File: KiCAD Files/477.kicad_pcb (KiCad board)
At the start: 2 copper layers, 96 x 57.4 mm, 75 parts, among them IC1 W25N01GVSFIG, IC2 W25N01GVSFIG, IC3 W25N01GVSFIG, IC4 W25N01GVSFIG, IC5 AZ1117IH-3.3TRG1, IC6 USBLC6-2SC6, J1 BM06B-SRSS-TBT_LF__SN_, J2 6364372-2, J3 TSW-103-14-S-D, J4 TSW-103-14-S-D, J5 BM07B-SRSS-TB_LF__SN_, J6 BM09B-SRSS-TB_LF__SN_, J7 TSW-105-05-F-S, U1 STM32H7A3RGTx, Y1 ABM8G-48.000MHZ-18-D2Y-T

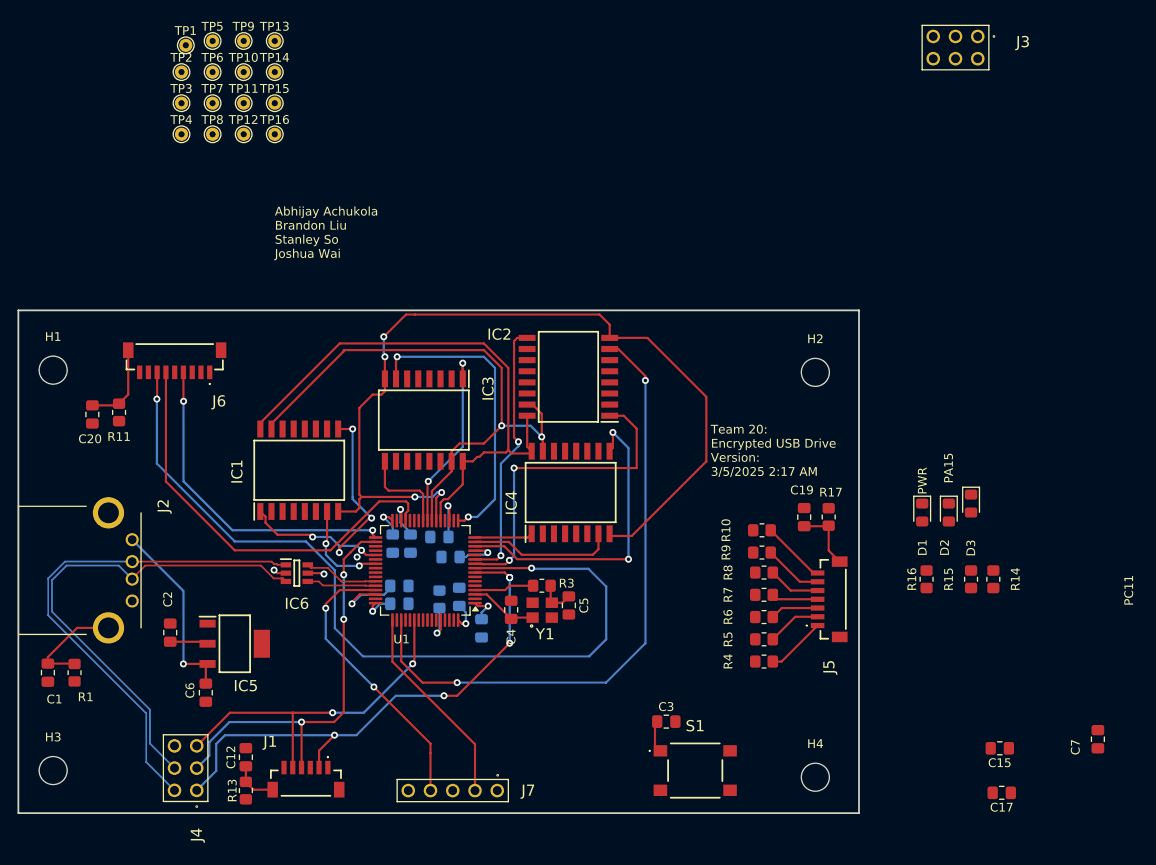
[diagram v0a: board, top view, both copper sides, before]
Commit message: added pcb routing for debug pins
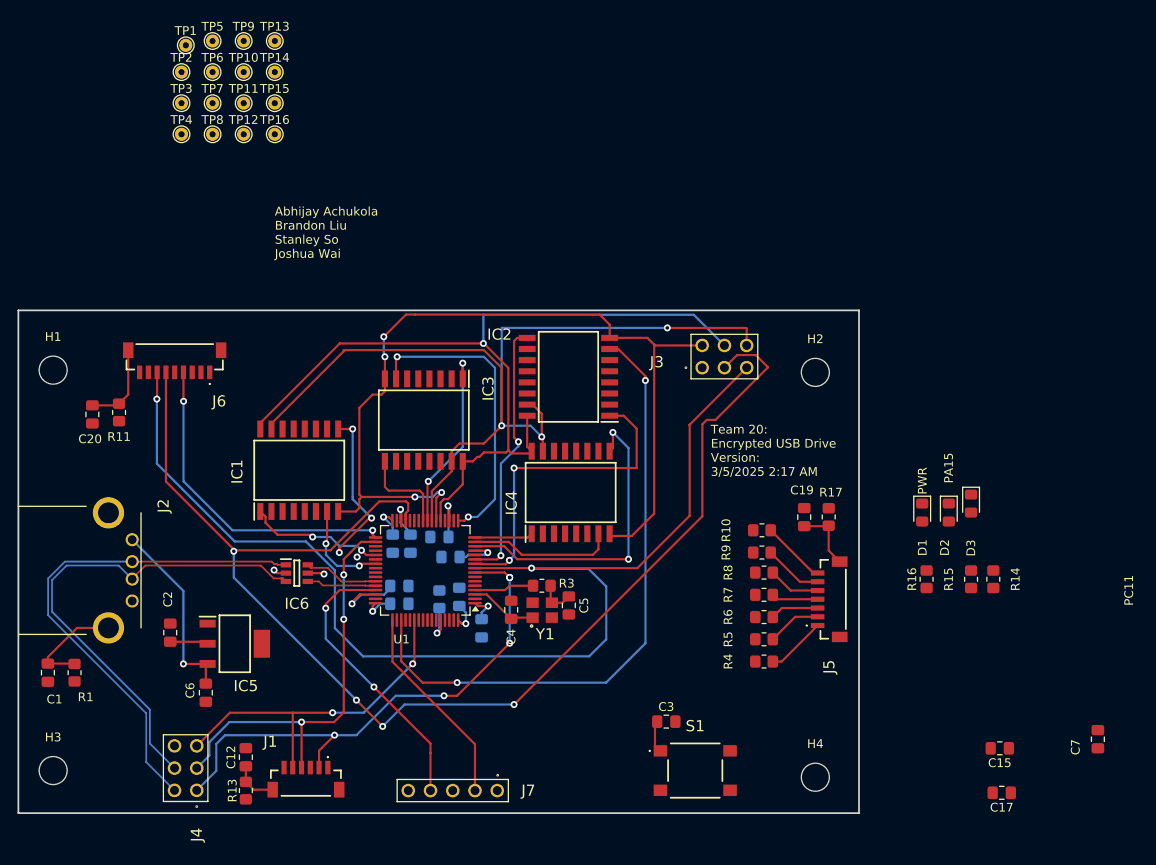
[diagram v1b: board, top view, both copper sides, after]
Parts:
- moved J3 49.2 mm to (219.0, 83.5), turned to 0 degrees
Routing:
- net PB10/LCD SCK: track 47.9 -> 148.2 mm, vias 0 -> 4
- net PA7/MOSI: track 65.5 -> 106.6 mm, vias 2 -> 3
- net PC1/LCD MOSI: track 97.5 -> 137.7 mm
- net PA5/SCK: track 64.2 -> 96.5 mm, vias 0 -> 1
- net PA6/MISO: track 101.7 -> 102.3 mm

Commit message: routed resistors, caps, leds
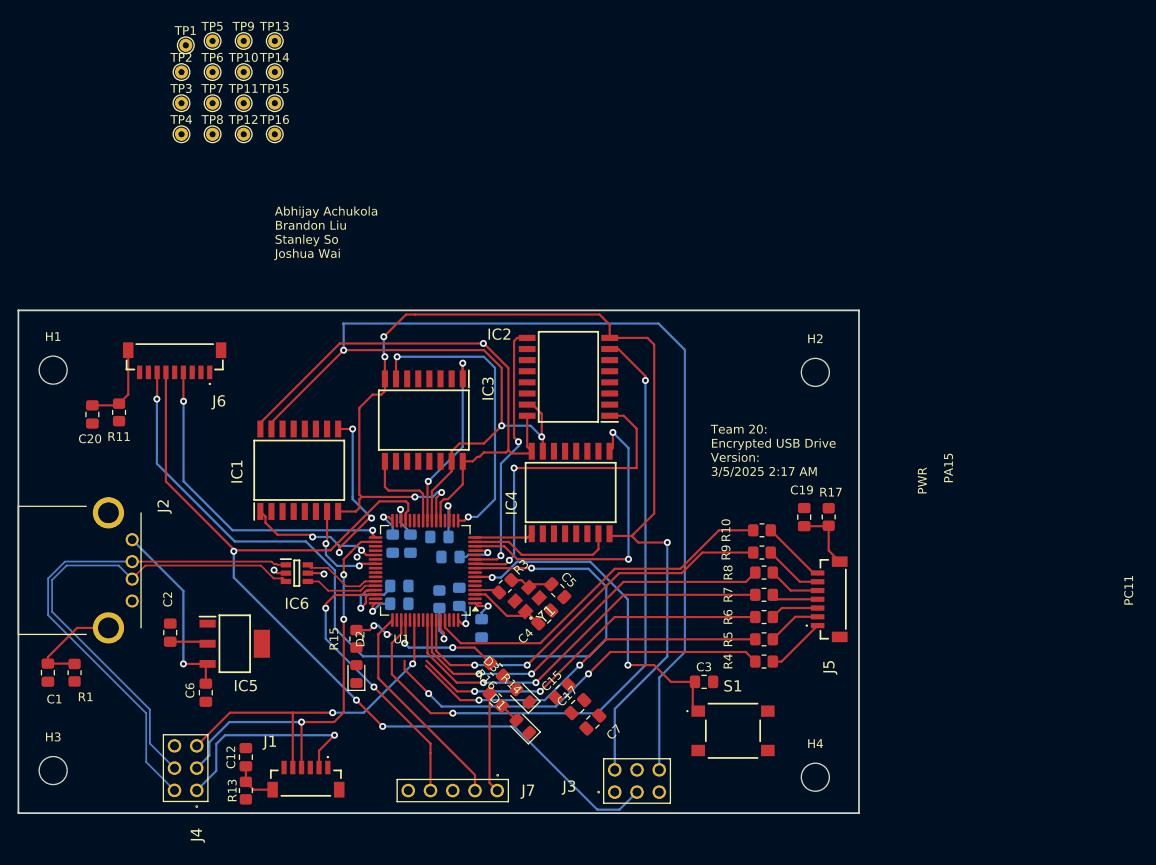
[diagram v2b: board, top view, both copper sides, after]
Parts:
- moved R15 70.5 mm to (179.5, 114.5)
- moved D2 70.1 mm to (179.5, 118.5), turned to 90 degrees
- moved R14 58.5 mm to (195.4, 121.4), turned to 135 degrees
- moved C7 57.7 mm to (206.5, 124.0), turned to 45 degrees
- moved D3 55.7 mm to (198.5, 121.0), turned to 135 degrees
- moved D1 51.7 mm to (198.5, 124.5), turned to 135 degrees
- moved C15 50.4 mm to (203.0, 120.5), turned to 45 degrees
- moved R16 50.2 mm to (195.5, 118.0), turned to 135 degrees
- moved J3 49.5 mm to (209.0, 132.0)
- moved C17 49.4 mm to (204.8, 122.2), turned to 45 degrees
- moved C3 6.26 mm to (219.2, 119.4)
- moved S1 6.26 mm to (222.5, 125.0)
- moved R3 4.18 mm to (196.5, 108.5), turned to -135 degrees
- moved C4 3.91 mm to (201.0, 112.0), turned to 45 degrees
- moved Y1 2.11 mm to (199.0, 110.0), turned to 45 degrees
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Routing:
- net PA7/MOSI: track 106.6 -> 158.0 mm
- net PB5/KeyR4: track 0.00 -> 46.8 mm, vias 0 -> 2
- net PB6/KeyC1: track 0.00 -> 46.4 mm, vias 0 -> 2
- net PB0/KeyR1: track 0.00 -> 45.8 mm, vias 0 -> 2
- net PB7/KeyC2: track 0.00 -> 45.7 mm, vias 0 -> 2
- net PB2/KeyR3: track 0.00 -> 42.5 mm, vias 0 -> 2
- net PB8/KeyC3: track 0.00 -> 42.1 mm
- net PB1/KeyR2: track 0.00 -> 42.1 mm, vias 0 -> 2
- net PC1/LCD MOSI: track 137.7 -> 97.5 mm
- net PB10/LCD SCK: track 148.2 -> 108.7 mm, vias 4 -> 3
- net PC0/Touch Out: track 60.6 -> 24.6 mm, vias 5 -> 1
- net nRST: track 2.97 -> 38.9 mm, vias 0 -> 2
- net PA5/SCK: track 96.5 -> 64.2 mm
- net PA6/MISO: track 102.3 -> 129.6 mm, vias 4 -> 5
- net PC11/Debug: track 0.00 -> 13.4 mm, vias 0 -> 2
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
